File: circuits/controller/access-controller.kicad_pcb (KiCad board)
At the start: 4 copper layers, 150 x 90 mm, 144 parts, among them J1 Conn_01x01_Female, J10 Terminal_01x03, J11 Terminal_01x04, J12 Screw_Terminal_01x05, J13 Conn_02x06_Odd_Even, J14 Terminal_01x04, J15 Terminal_01x03, J16 Terminal_01x03, J17 Terminal_01x03, J18 Terminal_01x04, J19 Screw_Terminal_01x05, J2 Conn_01x01_Female, J20 USB_MINI_B, J21 USB_MINI_B, J23 CONN_RJ45, J3 Conn_01x01_Female, J4 Conn_01x01_Female, J5 Barrel_Jack_Switch, J6 Screw_Terminal_01x02, J7 Terminal_01x04, J8 Terminal_01x03, J9 Terminal_01x03, Q1 Q_L8050QLT1G, Q10 Q_MMBT5551, Q11 Q_MMBT5551, Q12 Q_MMBT5551, Q13 Q_MMBT5551, Q14 Q_MMBT5551, Q15 Q_MMBT5551, Q2 Q_L8550HQLT1G, Q3 Q_MMBT5551, Q6 Q_MMBT5551, Q7 Q_MMBT5551, Q8 Q_AO3400A, Q9 Q_AO3400A, U1 MCP23017_SS, U10 TLP291-4, U12 W5500, U3 REG_AMS1117-3.3, U4 MIC29302WU, U5 TLP291-4, U6 CP2102N-Axx-xQFN28, U7 ESP32-S3-WROOM-1, U8 REG_MT2492, U9 TLP291-4

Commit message: sent to fab, revised
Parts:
- moved D4 183.2 mm to (153.4, 114.5)
- moved D3 151.7 mm to (131.3, 88.8), turned to 90 degrees
- moved D14 148.9 mm to (117.9, 93.7), turned to 180 degrees
- moved D15 146.2 mm to (117.9, 91.9), turned to 180 degrees
- moved D16 143.6 mm to (117.9, 90.1), turned to 180 degrees
- moved D17 141.1 mm to (117.9, 88.4), turned to 180 degrees
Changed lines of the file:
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@@
   )
   (footprint "LED_SMD:LED_0603_1608Metric" (layer "F.Cu")
-    (at 1.545 8.565)
+    (at 117.9 88.4 180)
     (descr "LED SMD 0603 (1608 Metric), square (rectangular) end terminal, IPC_7351 nominal, (Body size source: http://www.tortai-tech.com/upload/download/2011102023233369053.pdf), generated with kicad-footprint-generator")
     (tags "LED")
@@
     (property "Sheetname" "Ethernet")
     (attr smd)
-    (fp_text reference "D17" (at 0 -1.43) (layer "F.SilkS")
-        (effects (font (size 1 1) (thickness 0.15)))
+    (fp_text reference "D17" (at 2.85 -0.075) (layer "F.SilkS")
+        (effects (font (size 0.8 0.8) (thickness 0.15)))
     )
     (fp_text value "Red" (at 0 1.43) (layer "F.Fab")
@@
     (fp_line (start 0.8 0.4) (end 0.8 -0.4)
       (stroke (width 0.1) (type solid)) (layer "F.Fab"))
-    (pad "1" smd roundrect (at -0.7875 0) (size 0.875 0.95) (layers "F.Cu" "F.Paste" "F.Mask") (roundrect_rratio 0.25)
+    (pad "1" smd roundrect (at -0.7875 0 180) (size 0.875 0.95) (layers "F.Cu" "F.Paste" "F.Mask") (roundrect_rratio 0.25)
       (net 147 "Net-(D17-K)") (pinfunction "K") (pintype "passive"))
-    (pad "2" smd roundrect (at 0.7875 0) (size 0.875 0.95) (layers "F.Cu" "F.Paste" "F.Mask") (roundrect_rratio 0.25)
+    (pad "2" smd roundrect (at 0.7875 0 180) (size 0.875 0.95) (layers "F.Cu" "F.Paste" "F.Mask") (roundrect_rratio 0.25)
       (net 148 "Net-(D17-A)") (pinfunction "A") (pintype "passive"))
     (model "${KICAD6_3DMODEL_DIR}/LED_SMD.3dshapes/LED_0603_1608Metric.wrl"
@@
   )
   (footprint "LED_SMD:LED_0603_1608Metric_Pad1.05x0.95mm_HandSolder" (layer "F.Cu")
-    (at 7.77 0.795)
+    (at 131.35 88.8 90)
     (descr "LED SMD 0603 (1608 Metric), square (rectangular) end terminal, IPC_7351 nominal, (Body size source: http://www.tortai-tech.com/upload/download/2011102023233369053.pdf), generated with kicad-footprint-generator")
     (tags "LED handsolder")
@@
     (property "ki_description" "White 0603 Light Emitting Diodes (LED) ROHS\n")
     (attr smd)
-    (fp_text reference "D3" (at 0 -1.43) (layer "F.SilkS")
-        (effects (font (size 1 1) (thickness 0.15)))
+    (fp_text reference "D3" (at 2.325 -0.075 180) (layer "F.SilkS")
+        (effects (font (size 0.8 0.8) (thickness 0.15)))
     )
-    (fp_text value "White" (at 0 1.43) (layer "F.Fab")
+    (fp_text value "White" (at 0 1.43 90) (layer "F.Fab")
         (effects (font (size 1 1) (thickness 0.15)))
     )
-    (fp_text user "${REFERENCE}" (at 0 0) (layer "F.Fab")
+    (fp_text user "${REFERENCE}" (at 0 0 90) (layer "F.Fab")
         (effects (font (size 0.4 0.4) (thickness 0.06)))
     )
@@
     (fp_line (start 0.8 0.4) (end 0.8 -0.4)
       (stroke (width 0.1) (type solid)) (layer "F.Fab"))
-    (pad "1" smd roundrect (at -0.875 0) (size 1.05 0.95) (layers "F.Cu" "F.Paste" "F.Mask") (roundrect_rratio 0.25)
+    (pad "1" smd roundrect (at -0.875 0 90) (size 1.05 0.95) (layers "F.Cu" "F.Paste" "F.Mask") (roundrect_rratio 0.25)
       (net 34 "Net-(D3-K)") (pinfunction "K") (pintype "passive"))
-    (pad "2" smd roundrect (at 0.875 0) (size 1.05 0.95) (layers "F.Cu" "F.Paste" "F.Mask") (roundrect_rratio 0.25)
+    (pad "2" smd roundrect (at 0.875 0 90) (size 1.05 0.95) (layers "F.Cu" "F.Paste" "F.Mask") (roundrect_rratio 0.25)
       (net 167 "/3V3") (pinfunction "A") (pintype "passive"))
     (model "${KICAD6_3DMODEL_DIR}/LED_SMD.3dshapes/LED_0603_1608Metric.wrl"
@@
   )
   (footprint "LED_SMD:LED_0603_1608Metric_Pad1.05x0.95mm_HandSolder" (layer "F.Cu")
-    (at 7.77 3.385)
+    (at 153.425 114.5)
     (descr "LED SMD 0603 (1608 Metric), square (rectangular) end terminal, IPC_7351 nominal, (Body size source: http://www.tortai-tech.com/upload/download/2011102023233369053.pdf), generated with kicad-footprint-generator")
     (tags "LED handsolder")
@@
     (property "ki_description" "White 0603 Light Emitting Diodes (LED) ROHS\n")
     (attr smd)
-    (fp_text reference "D4" (at 0 -1.43) (layer "F.SilkS")
-        (effects (font (size 1 1) (thickness 0.15)))
+    (fp_text reference "D4" (at 0.025 1.45) (layer "F.SilkS")
+        (effects (font (size 0.8 0.8) (thickness 0.15)))
     )
     (fp_text value "White" (at 0 1.43) (layer "F.Fab")
@@
   )
   (footprint "LED_SMD:LED_0603_1608Metric" (layer "F.Cu")
-    (at 1.545 3.385)
+    (at 117.9 91.9 180)
     (descr "LED SMD 0603 (1608 Metric), square (rectangular) end terminal, IPC_7351 nominal, (Body size source: http://www.tortai-tech.com/upload/download/2011102023233369053.pdf), generated with kicad-footprint-generator")
     (tags "LED")
@@
     (property "Sheetname" "Ethernet")
     (attr smd)
-    (fp_text reference "D15" (at 0 -1.43) (layer "F.SilkS")
-        (effects (font (size 1 1) (thickness 0.15)))
+    (fp_text reference "D15" (at 2.6875 -0.1) (layer "F.SilkS")
+        (effects (font (size 0.8 0.8) (thickness 0.15)))
     )
     (fp_text value "Red" (at 0 1.43) (layer "F.Fab")
@@
     (fp_line (start 0.8 0.4) (end 0.8 -0.4)
       (stroke (width 0.1) (type solid)) (layer "F.Fab"))
-    (pad "1" smd roundrect (at -0.7875 0) (size 0.875 0.95) (layers "F.Cu" "F.Paste" "F.Mask") (roundrect_rratio 0.25)
+    (pad "1" smd roundrect (at -0.7875 0 180) (size 0.875 0.95) (layers "F.Cu" "F.Paste" "F.Mask") (roundrect_rratio 0.25)
       (net 143 "Net-(D15-K)") (pinfunction "K") (pintype "passive"))
-    (pad "2" smd roundrect (at 0.7875 0) (size 0.875 0.95) (layers "F.Cu" "F.Paste" "F.Mask") (roundrect_rratio 0.25)
+    (pad "2" smd roundrect (at 0.7875 0 180) (size 0.875 0.95) (layers "F.Cu" "F.Paste" "F.Mask") (roundrect_rratio 0.25)
       (net 144 "Net-(D15-A)") (pinfunction "A") (pintype "passive"))
     (model "${KICAD6_3DMODEL_DIR}/LED_SMD.3dshapes/LED_0603_1608Metric.wrl"
@@
     (attr through_hole)
     (fp_text reference "J5" (at -8.45 5.75) (layer "F.SilkS")
-        (effects (font (size 1 1) (thickness 0.15)))
+        (effects (font (size 0.8 0.8) (thickness 0.15)))
     )
     (fp_text value "Barrel_Jack_Switch" (at -6.2 -5.5) (layer "F.Fab")
@@
   )
   (footprint "LED_SMD:LED_0603_1608Metric" (layer "F.Cu")
-    (at 1.545 5.975)
+    (at 117.9 90.1 180)
     (descr "LED SMD 0603 (1608 Metric), square (rectangular) end terminal, IPC_7351 nominal, (Body size source: http://www.tortai-tech.com/upload/download/2011102023233369053.pdf), generated with kicad-footprint-generator")
     (tags "LED")
@@
     (property "Sheetname" "Ethernet")
     (attr smd)
-    (fp_text reference "D16" (at 0 -1.43) (layer "F.SilkS")
-        (effects (font (size 1 1) (thickness 0.15)))
+    (fp_text reference "D16" (at 2.6 0) (layer "F.SilkS")
+        (effects (font (size 0.8 0.8) (thickness 0.15)))
     )
     (fp_text value "Red" (at 0 1.43) (layer "F.Fab")
@@
     (fp_line (start 0.8 0.4) (end 0.8 -0.4)
       (stroke (width 0.1) (type solid)) (layer "F.Fab"))
-    (pad "1" smd roundrect (at -0.7875 0) (size 0.875 0.95) (layers "F.Cu" "F.Paste" "F.Mask") (roundrect_rratio 0.25)
+    (pad "1" smd roundrect (at -0.7875 0 180) (size 0.875 0.95) (layers "F.Cu" "F.Paste" "F.Mask") (roundrect_rratio 0.25)
       (net 145 "Net-(D16-K)") (pinfunction "K") (pintype "passive"))
-    (pad "2" smd roundrect (at 0.7875 0) (size 0.875 0.95) (layers "F.Cu" "F.Paste" "F.Mask") (roundrect_rratio 0.25)
+    (pad "2" smd roundrect (at 0.7875 0 180) (size 0.875 0.95) (layers "F.Cu" "F.Paste" "F.Mask") (roundrect_rratio 0.25)
       (net 146 "Net-(D16-A)") (pinfunction "A") (pintype "passive"))
     (model "${KICAD6_3DMODEL_DIR}/LED_SMD.3dshapes/LED_0603_1608Metric.wrl"
@@
   )
   (footprint "LED_SMD:LED_0603_1608Metric" (layer "F.Cu")
-    (at 1.545 0.795)
+    (at 117.9 93.7 180)
     (descr "LED SMD 0603 (1608 Metric), square (rectangular) end terminal, IPC_7351 nominal, (Body size source: http://www.tortai-tech.com/upload/download/2011102023233369053.pdf), generated with kicad-footprint-generator")
     (tags "LED")
@@
     (property "Sheetname" "Ethernet")
     (attr smd)
-    (fp_text reference "D14" (at 0 -1.43) (layer "F.SilkS")
-        (effects (font (size 1 1) (thickness 0.15)))
+    (fp_text reference "D14" (at 2.7875 -0.1) (layer "F.SilkS")
+        (effects (font (size 0.8 0.8) (thickness 0.15)))
     )
     (fp_text value "Red" (at 0 1.43) (layer "F.Fab")
@@
     (fp_line (start 0.8 0.4) (end 0.8 -0.4)
       (stroke (width 0.1) (type solid)) (layer "F.Fab"))
-    (pad "1" smd roundrect (at -0.7875 0) (size 0.875 0.95) (layers "F.Cu" "F.Paste" "F.Mask") (roundrect_rratio 0.25)
+    (pad "1" smd roundrect (at -0.7875 0 180) (size 0.875 0.95) (layers "F.Cu" "F.Paste" "F.Mask") (roundrect_rratio 0.25)
       (net 141 "Net-(D14-K)") (pinfunction "K") (pintype "passive"))
-    (pad "2" smd roundrect (at 0.7875 0) (size 0.875 0.95) (layers "F.Cu" "F.Paste" "F.Mask") (roundrect_rratio 0.25)
+    (pad "2" smd roundrect (at 0.7875 0 180) (size 0.875 0.95) (layers "F.Cu" "F.Paste" "F.Mask") (roundrect_rratio 0.25)
       (net 142 "Net-(D14-A)") (pinfunction "A") (pintype "passive"))
     (model "${KICAD6_3DMODEL_DIR}/LED_SMD.3dshapes/LED_0603_1608Metric.wrl"

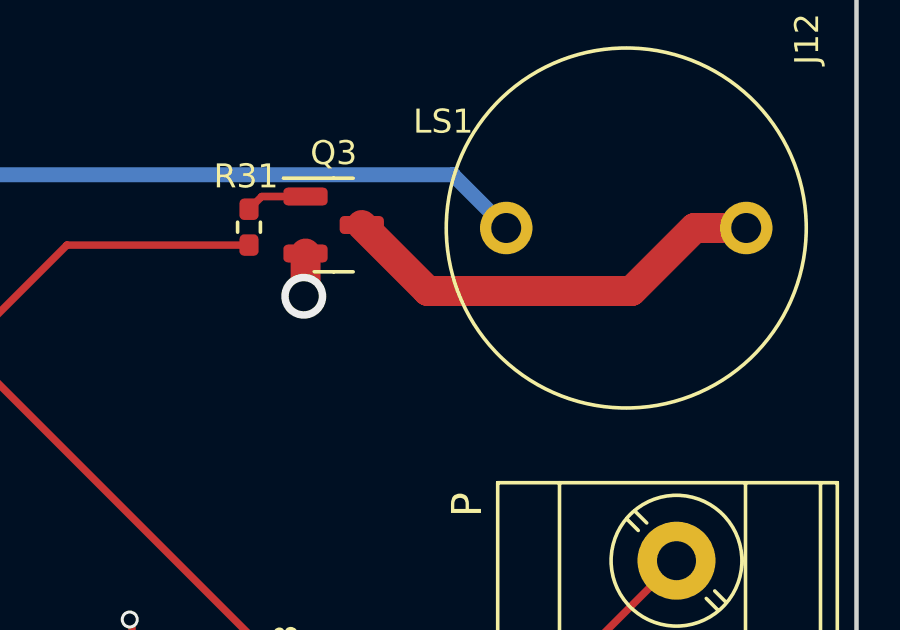
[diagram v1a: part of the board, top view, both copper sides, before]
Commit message: added polarity to speaker, added lcsc part for header
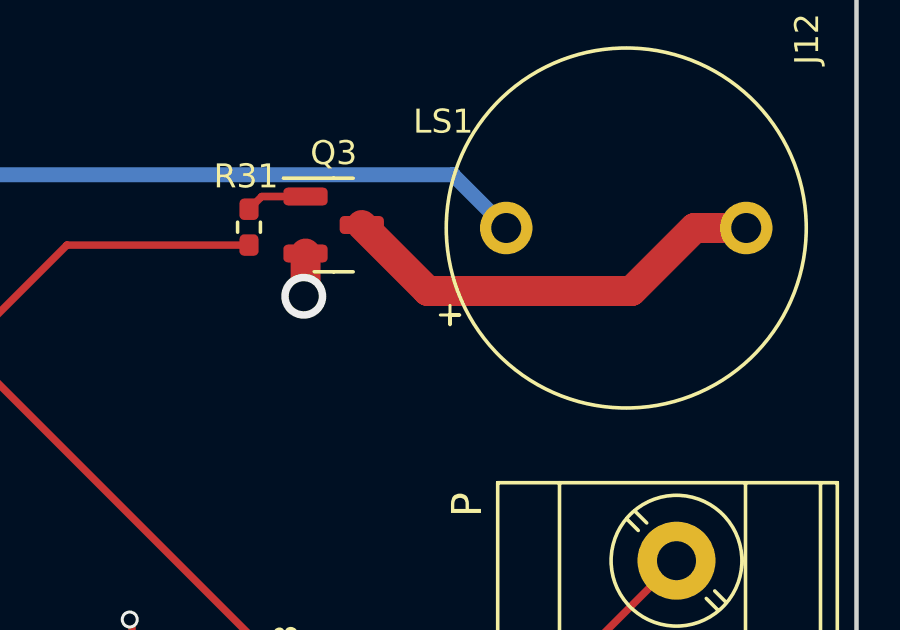
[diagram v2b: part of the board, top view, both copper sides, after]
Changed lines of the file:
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@@
         (effects (font (size 1 1) (thickness 0.15)))
     )
+    (fp_line (start -3.225 -5.875) (end -2.575 -5.875)
+      (stroke (width 0.1) (type default)) (layer "F.SilkS"))
+    (fp_line (start -2.9 -6.2) (end -2.9 -5.55)
+      (stroke (width 0.1) (type default)) (layer "F.SilkS"))
+    (fp_line (start -2.9 -5.875) (end -3.225 -5.875)
+      (stroke (width 0.1) (type default)) (layer "F.SilkS"))
+    (fp_line (start -2.9 -5.55) (end -2.9 -5.875)
+      (stroke (width 0.1) (type default)) (layer "F.SilkS"))
     (fp_circle (center 0 0) (end 6 0)
       (stroke (width 0.12) (type solid)) (fill none) (layer "F.SilkS"))

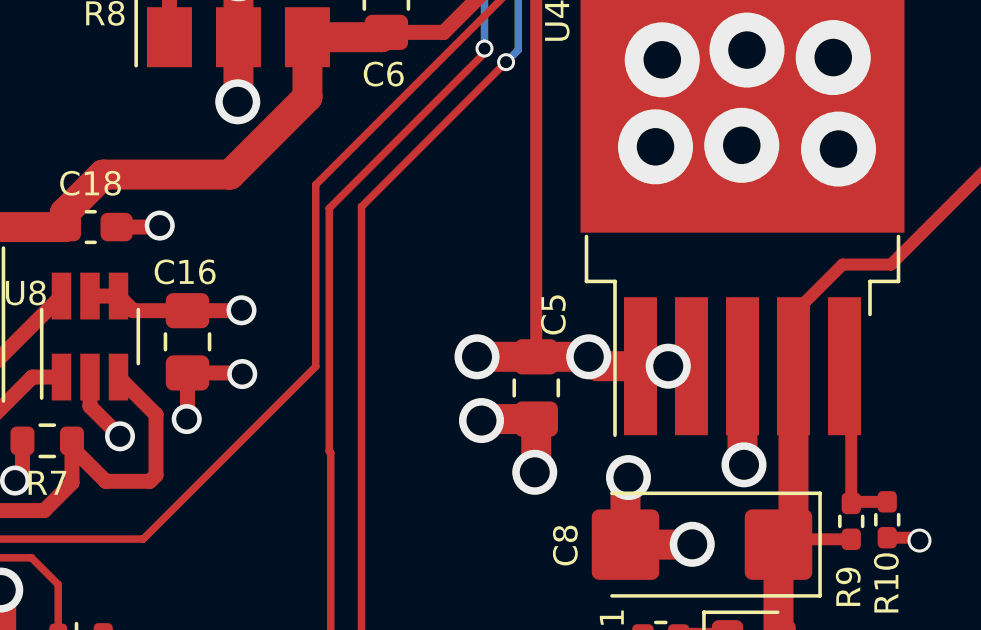
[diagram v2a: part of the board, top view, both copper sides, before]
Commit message: powering 5v reg from 12v reg
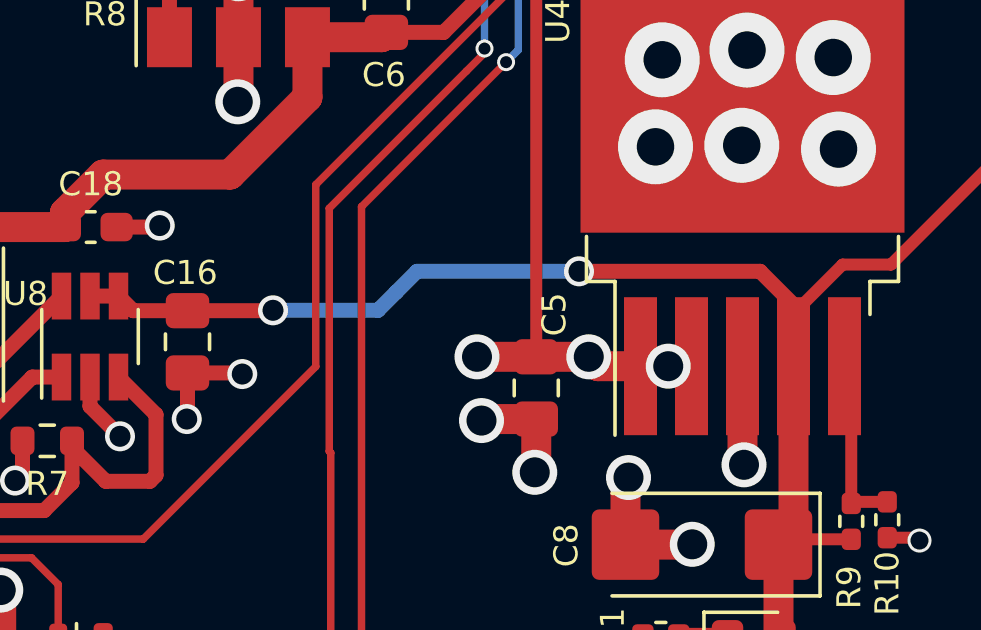
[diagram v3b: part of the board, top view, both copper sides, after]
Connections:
- C16 pad 1: /POWER -> /REG_POWER
- U8 pad 4: /POWER -> /REG_POWER
- U8 pad 5: /POWER -> /REG_POWER
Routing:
- net /REG_POWER: track 129.7 -> 156.4 mm, vias 1 -> 3
- net /POWER: track 60.7 -> 55.5 mm, vias 10 -> 9
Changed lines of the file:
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@@
     (descr "surface-mounted straight pin header, 2x06, 2.54mm pitch, double rows")
     (tags "Surface mounted pin header SMD 2x06 2.54mm double row")
+    (property "LCSC" "C2884015")
+    (property "Part Number" "X6521WVS-2x06H-C60D74")
     (property "Sheetfile" "access-controller.kicad_sch")
     (property "Sheetname" "")
-    (property "ki_description" "Generic connector, double row, 02x06, odd/even pin numbering scheme (row 1 odd numbers, row 2 even numbers), script generated (kicad-library-utils/schlib/autogen/connector/)")
+    (property "ki_description" "Gold 250V 3A Brick nogging Square Pins 2.5mm 12P 260℃ 6mm -40℃~+105℃ 2.54mm 双排 Black Brass 2x6P SMD,P=2.54mm,Surface Mount，Right Angle Pin Headers ROHS\n")
     (property "ki_keywords" "connector")
     (attr smd)
@@
       (net 174 "Net-(U8-FB)") (pinfunction "FB") (pintype "input"))
     (pad "4" smd rect (at 1.35 0.95 90) (size 1.56 0.65) (layers "F.Cu" "F.Paste" "F.Mask")
-      (net 8 "/POWER") (pinfunction "EN") (pintype "input"))
+      (net 9 "/REG_POWER") (pinfunction "EN") (pintype "input"))
     (pad "5" smd rect (at 1.35 0 90) (size 1.56 0.65) (layers "F.Cu" "F.Paste" "F.Mask")
-      (net 8 "/POWER") (pinfunction "VIN") (pintype "power_in"))
+      (net 9 "/REG_POWER") (pinfunction "VIN") (pintype "power_in"))
     (pad "6" smd rect (at 1.35 -0.95 90) (size 1.56 0.65) (layers "F.Cu" "F.Paste" "F.Mask")
       (net 173 "Net-(U8-SW)") (pinfunction "SW") (pintype "power_out"))
@@
       (stroke (width 0.1) (type solid)) (layer "F.Fab"))
     (pad "1" smd roundrect (at -1.0375 0 270) (size 1.175 1.45) (layers "F.Cu" "F.Paste" "F.Mask") (roundrect_rratio 0.2127659574)
-      (net 8 "/POWER") (pintype "passive"))
+      (net 9 "/REG_POWER") (pintype "passive"))
     (pad "2" smd roundrect (at 1.0375 0 270) (size 1.175 1.45) (layers "F.Cu" "F.Paste" "F.Mask") (roundrect_rratio 0.2127659574)
       (net 1 "GND") (pintype "passive"))
@@
   (segment (start 112.275 74.025) (end 112.275 66.6) (width 0.25) (layer "B.Cu") (net 3))
   (segment (start 112.275 66.6) (end 112.625 66.25) (width 0.25) (layer "B.Cu") (net 3))
-  (segment (start 134.55 103.7125) (end 136.3375 103.7125) (width 0.5) (layer "F.Cu") (net 8))
-  (segment (start 136.3375 103.7125) (end 136.35 103.7) (width 0.5) (layer "F.Cu") (net 8))
   (segment (start 99.1 104.895) (end 100.195 104.895) (width 0.25) (layer "F.Cu") (net 8))
   (segment (start 100.4 118.45) (end 100.425 118.475) (width 1) (layer "F.Cu") (net 8))
-  (segment (start 134.55 103.7125) (end 132.7375 103.7125) (width 0.5) (layer "F.Cu") (net 8))
-  (segment (start 132.7375 103.7125) (end 132.25 103.225) (width 0.5) (layer "F.Cu") (net 8))
   (segment (start 106.5175 118.2925) (end 106.575 118.35) (width 1) (layer "F.Cu") (net 8))
-  (segment (start 131.3 103.225) (end 132.25 103.225) (width 0.5) (layer "F.Cu") (net 8))
   (segment (start 146.175 91.3) (end 146.175 105.25) (width 0.4) (layer "F.Cu") (net 8))
   (segment (start 149.65 105.5625) (end 148.2375 105.5625) (width 1) (layer "F.Cu") (net 8))
@@
   (via (at 103.425 104.7) (size 1.5) (drill 1) (layers "F.Cu" "B.Cu") (net 8))
   (via (at 106.575 118.35) (size 1.5) (drill 1) (layers "F.Cu" "B.Cu") (net 8))
-  (via (at 136.35 103.7) (size 1) (drill 0.7) (layers "F.Cu" "B.Cu") (net 8))
   (via (at 144.2 105.25) (size 1.5) (drill 1) (layers "F.Cu" "B.Cu") (net 8))
   (via (at 109.65 104.725) (size 1.5) (drill 1) (layers "F.Cu" "B.Cu") (net 8))
@@
   (segment (start 129.125 129.6) (end 129.125 127.2) (width 0.25) (layer "F.Cu") (net 9))
   (segment (start 163.93 96.245) (end 163.93 93.5) (width 0.4) (layer "F.Cu") (net 9))
+  (segment (start 147.6 102.4) (end 153.6375 102.4) (width 0.5) (layer "F.Cu") (net 9))
+  (segment (start 153.6375 102.4) (end 154.75 103.5125) (width 0.5) (layer "F.Cu") (net 9))
   (segment (start 129.125 127.2) (end 131.74 124.585) (width 0.25) (layer "F.Cu") (net 9))
+  (segment (start 134.55 103.7125) (end 132.7375 103.7125) (width 0.5) (layer "F.Cu") (net 9))
+  (segment (start 132.7375 103.7125) (end 132.25 103.225) (width 0.5) (layer "F.Cu") (net 9))
   (segment (start 159.575 131.975) (end 162.5 129.05) (width 1) (layer "F.Cu") (net 9))
+  (segment (start 137.3875 103.7125) (end 137.4 103.7) (width 0.5) (layer "F.Cu") (net 9))
   (segment (start 154.35 120.9) (end 162.5 129.05) (width 1) (layer "F.Cu") (net 9))
+  (segment (start 134.55 103.7125) (end 137.3875 103.7125) (width 0.5) (layer "F.Cu") (net 9))
   (segment (start 154.35 114.785) (end 154.35 120.9) (width 1) (layer "F.Cu") (net 9))
   (segment (start 154.75 105.5625) (end 154.75 103.8125) (width 0.4) (layer "F.Cu") (net 9))
   (segment (start 158 102.175) (end 163.93 96.245) (width 0.4) (layer "F.Cu") (net 9))
+  (segment (start 131.3 103.225) (end 132.25 103.225) (width 0.5) (layer "F.Cu") (net 9))
   (segment (start 138.95 131.575) (end 131.1 131.575) (width 0.25) (layer "F.Cu") (net 9))
   (segment (start 144.3 129.05) (end 141.475 129.05) (width 0.25) (layer "F.Cu") (net 9))
+  (segment (start 154.75 103.5125) (end 154.75 105.5625) (width 0.5) (layer "F.Cu") (net 9))
   (segment (start 156.3875 102.175) (end 158 102.175) (width 0.4) (layer "F.Cu") (net 9))
   (segment (start 129.7 61.575) (end 130.975 60.3) (width 0.25) (layer "F.Cu") (net 9))
@@
   (segment (start 144.3 129.05) (end 147.225 131.975) (width 1) (layer "F.Cu") (net 9))
   (via (at 130.975 60.3) (size 0.6) (drill 0.4) (layers "F.Cu" "B.Cu") (net 9))
+  (via (at 147.6 102.4) (size 1) (drill 0.7) (layers "F.Cu" "B.Cu") (net 9))
+  (via (at 137.4 103.7) (size 1) (drill 0.7) (layers "F.Cu" "B.Cu") (net 9))
+  (segment (start 141.5 103.1) (end 142.2 102.4) (width 0.5) (layer "B.Cu") (net 9))
+  (segment (start 142.2 102.4) (end 147.6 102.4) (width 0.5) (layer "B.Cu") (net 9))
+  (segment (start 137.4 103.7) (end 140.9 103.7) (width 0.5) (layer "B.Cu") (net 9))
   (segment (start 130.975 60.3) (end 135.875 55.4) (width 0.25) (layer "B.Cu") (net 9))
+  (segment (start 140.9 103.7) (end 141.5 103.1) (width 0.5) (layer "B.Cu") (net 9))
   (segment (start 149.71 55.4) (end 154.46 50.65) (width 0.25) (layer "B.Cu") (net 9))
   (segment (start 135.875 55.4) (end 149.71 55.4) (width 0.25) (layer "B.Cu") (net 9))
